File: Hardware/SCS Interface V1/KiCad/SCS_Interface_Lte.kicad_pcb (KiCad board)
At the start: 2 copper layers, 22.2 x 39.4 mm, 23 parts, among them J1 SCS, J2 Conn_01x04, Q1 MMBTA06, Q2 MMBTA06

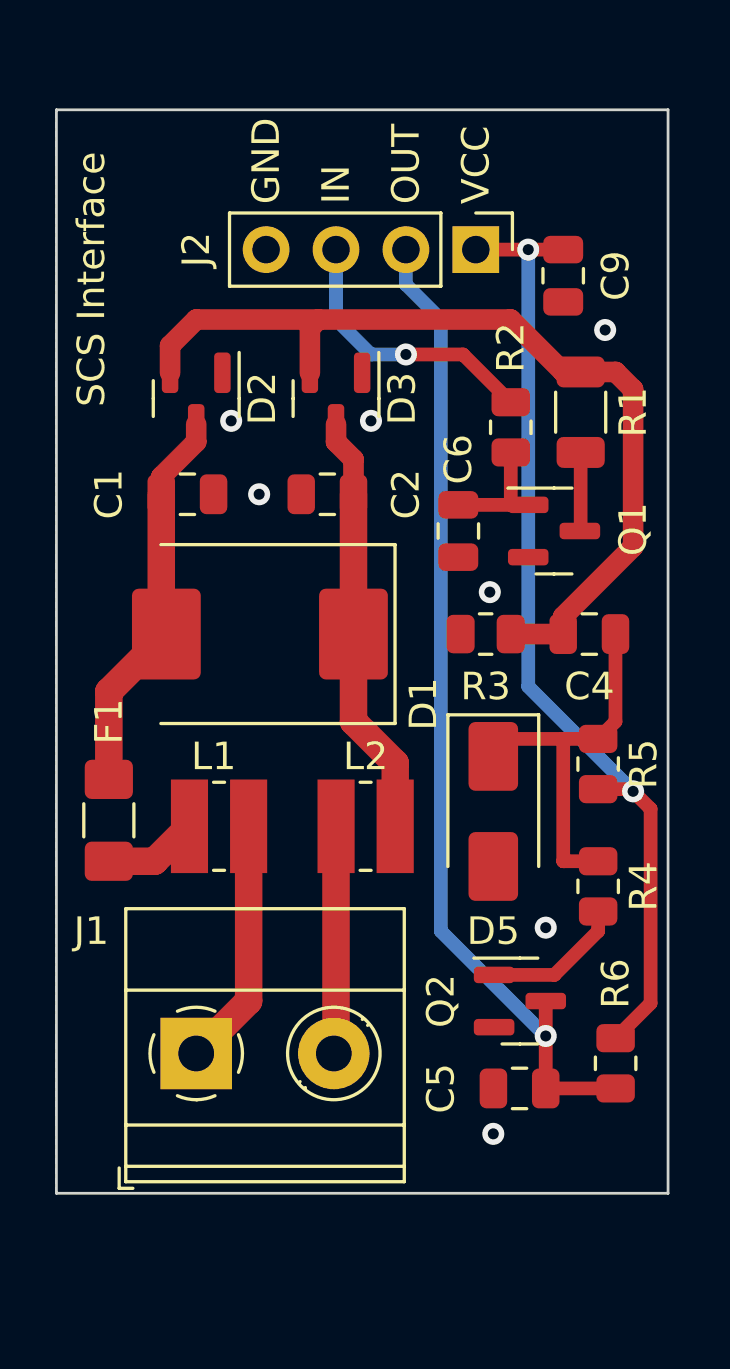
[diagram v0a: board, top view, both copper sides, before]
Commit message: Update PCB after first pcb build
- Replace input detection
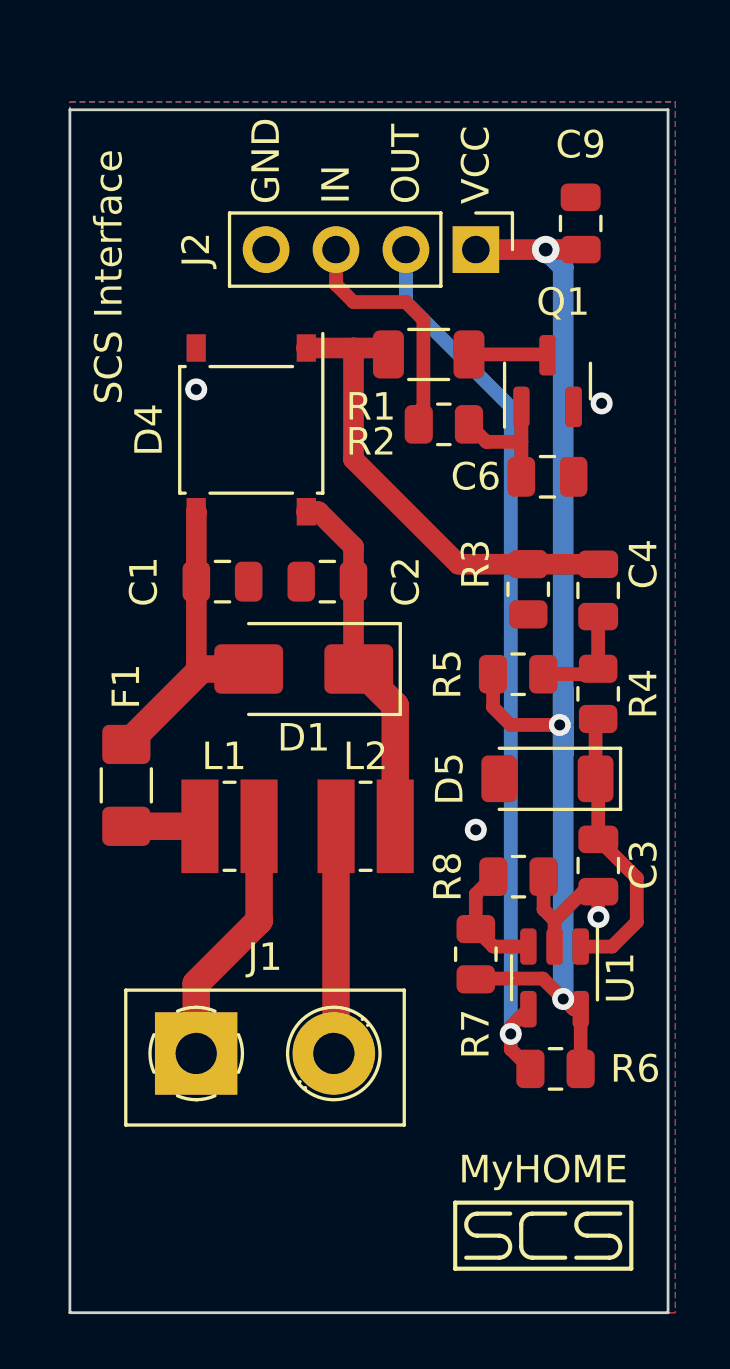
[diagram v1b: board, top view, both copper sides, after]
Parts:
- removed C5: 1n, Capacitor_SMD:C_0805_2012Metric
- removed D2, D3: BAS31, Package_TO_SOT_SMD:SOT-23
- removed Q2: MMBTA06, Package_TO_SOT_SMD:SOT-23
- added C3: 13p (OPT), Capacitor_SMD:C_0805_2012Metric, F.Cu at (163.2, 61.8)
- added D4: ABS2, Diode_SMD:Diode_Bridge_Diotec_ABS, F.Cu at (150.6, 45.9)
- added R7: 20k, Resistor_SMD:R_0805_2012Metric, F.Cu at (158.8, 65.0)
- added R8: 10k, Resistor_SMD:R_0805_2012Metric, F.Cu at (160.3, 62.2)
- added U1: LM397, Package_TO_SOT_SMD:SOT-23-5, F.Cu at (161.6, 65.8)
- D1: value TPSMC33A -> P4SMA39CA; footprint Diode_SMD:D_SMC -> Diode_SMD:D_SMA
- D5: value M2 -> FDLL4148; footprint Diode_SMD:D_SMA -> Diode_SMD:D_MiniMELF
- J1: footprint TerminalBlock_Phoenix:TerminalBlock_Phoenix_MKDS-1,5-2_1x02_P5.00mm_Horizontal -> TerminalBlock_Phoenix:TerminalBlock_Phoenix_MKDS-1,5-2_1x02_P5.00mm_Horizontal_PNP
- R4: value 100k -> 10k
- moved R4 6.99 mm to (163.2, 55.5)
- moved R1 5.91 mm to (157.0, 43.2), turned to 0 degrees
- moved Q1 5.45 mm to (161.4, 44.1), turned to 90 degrees
- moved R5 4.37 mm to (160.3, 54.8), turned to 180 degrees
- moved C6 3.79 mm to (161.4, 47.6), turned to 180 degrees
- moved C1 3.42 mm to (149.5, 51.4)
- moved C2 3.18 mm to (153.4, 51.4)
- moved R2 2.43 mm to (157.6, 45.7), turned to 0 degrees
- moved D5 2.29 mm to (161.3, 58.6), turned to 180 degrees
- moved R3 2.25 mm to (160.7, 51.7), turned to -90 degrees
- moved R6 2.19 mm to (161.6, 69.1), turned to 0 degrees
- moved D1 2.03 mm to (152.5, 54.6)
- moved C9 2.00 mm to (162.6, 38.4), turned to -90 degrees
- moved C4 1.62 mm to (163.2, 51.8), turned to -90 degrees
- moved F1 1.42 mm to (146.1, 58.8)
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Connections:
- C4 pad 2: Net-(D5-K) -> Net-(C4-Pad2)
- R4 pad 1: Net-(D5-K) -> Net-(C4-Pad2)
- R4 pad 2: Net-(Q2-B) -> Net-(D5-K)
- R5 pad 1: Net-(D5-K) -> Net-(C4-Pad2)
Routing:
- net SCS_BUS_CC: track 33.2 -> 17.6 mm
- net +3V3: track 35.5 -> 44.0 mm, vias 2 -> 3
- net GND: track 0.00 -> 5.65 mm, vias 7 -> 4
- net Net-(Q2-B): track 5.15 -> 0.00 mm
- net Net-(U1-+): track 0.00 -> 4.34 mm
- net Net-(C4-Pad2): track 0.00 -> 3.97 mm
- net SCS_OUT: track 36.4 -> 32.8 mm
- net Net-(D5-K): track 13.9 -> 10.4 mm
- net Net-(D1-A2): track 14.4 -> 11.4 mm
- net Net-(D1-A1): track 15.5 -> 13.0 mm
- net SCS_IN: track 10.1 -> 8.85 mm, vias 1 -> 0
- net Net-(F1-Pad1): track 3.46 -> 2.68 mm
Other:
- board size 22.2 x 39.4 mm -> 21.7 x 43.7 mm
- board text added: "MyHOME"
